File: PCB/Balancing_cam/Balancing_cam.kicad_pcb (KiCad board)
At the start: 4 copper layers, 50 x 50 mm, 123 parts, among them J1 JST_PH, J2 JST_PH, J3 USB_C_Receptacle_USB2.0_16P, J4 JST_XH, J5 Conn_01x04, J6 Conn_01x04, J7 Conn_01x04, J8 Conn_01x03, J9 Conn_01x04, Q1 BC817, SW1 SW_SPDT, SW2 EN, SW3 BOOT, U1 TMC2209-LA, U2 TMC2209-LA, U3 TPS62933, U4 TPS62933, U5 USBLC6-2P6, U6 LSM6DS3, U7 ESP32-S3-MINI-1

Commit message: Done, and completed bom
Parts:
- added TP1: TestPoint, TestPoint:TestPoint_Pad_D1.5mm, B.Cu at (141.1, 137.2)
- added TP10: TestPoint, TestPoint:TestPoint_Pad_D1.5mm, B.Cu at (139.4, 120.2)
- added TP11: TestPoint, TestPoint:TestPoint_Pad_D1.5mm, B.Cu at (136.2, 117.8)
- added TP12: TestPoint, TestPoint:TestPoint_Pad_D1.5mm, B.Cu at (109.8, 131.5)
- added TP13: TestPoint, TestPoint:TestPoint_Pad_D1.5mm, B.Cu at (109.0, 135.1)
- added TP14: TestPoint, TestPoint:TestPoint_Pad_D1.5mm, B.Cu at (126.2, 116.2)
- added TP15: TestPoint, TestPoint:TestPoint_Pad_D1.5mm, B.Cu at (107.8, 137.3)
- added TP16: TestPoint, TestPoint:TestPoint_Pad_D1.5mm, B.Cu at (130.3, 116.0)
- added TP17: TestPoint, TestPoint:TestPoint_Pad_D1.5mm, B.Cu at (128.4, 114.3)
- added TP18: TestPoint, TestPoint:TestPoint_Pad_D1.5mm, B.Cu at (115.0, 123.2)
- added TP19: TestPoint, TestPoint:TestPoint_Pad_D1.5mm, B.Cu at (115.0, 125.5)
- added TP2: TestPoint, TestPoint:TestPoint_Pad_D1.5mm, B.Cu at (141.1, 131.3)
- added TP21: TestPoint, TestPoint:TestPoint_Pad_D1.5mm, B.Cu at (114.3, 134.8)
- added TP22: TestPoint, TestPoint:TestPoint_Pad_D1.5mm, B.Cu at (121.6, 114.3)
- added TP23: TestPoint, TestPoint:TestPoint_Pad_D1.5mm, B.Cu at (123.8, 115.7)
- added TP3: TestPoint, TestPoint:TestPoint_Pad_D1.5mm, B.Cu at (120.0, 123.5)
- added TP4: TestPoint, TestPoint:TestPoint_Pad_D1.5mm, B.Cu at (132.5, 114.6)
- added TP5: TestPoint, TestPoint:TestPoint_Pad_D1.5mm, B.Cu at (146.8, 112.4)
- added TP6: TestPoint, TestPoint:TestPoint_Pad_D1.5mm, B.Cu at (132.5, 109.6)
- added TP7: TestPoint, TestPoint:TestPoint_Pad_D1.5mm, B.Cu at (132.5, 112.1)
- added TP8: TestPoint, TestPoint:TestPoint_Pad_D1.5mm, B.Cu at (108.7, 120.3)
- added TP9: TestPoint, TestPoint:TestPoint_Pad_D1.5mm, B.Cu at (108.7, 117.8)
- J1, J2: footprint Connector_JST:JST_PH_S2B-PH-SM4-TB_1x02-1MP_P2.00mm_Horizontal -> footprints:JST_PH_S2B-PH-SM4-TB_1x02-1MP_P2.00mm_Horizontal
- SW2: value EN -> B3U-1000P
- SW3: value BOOT -> B3U-1000P
- renumbered C45 to C29, C46 to C30, C29 to C31, C30 to C32, C31 to C33, C32 to C34, C33 to C35, C34 to C36, C35 to C37, C36 to C38, C37 to C39, C38 to C40, C39 to C41, C40 to C42, C41 to C43, C42 to C44, C43 to C45, C44 to C46, L9 to L10, L10 to L11, L11 to L12, L12 to L13, L13 to L14, L14 to L4, L4 to L5, L5 to L6, L6 to L7, L7 to L8, L8 to L9, R25 to R12, R12 to R13, R13 to R14, R14 to R15, R15 to R16, R16 to R17, R17 to R18, R18 to R19, R19 to R20, R20 to R21, R21 to R22, R22 to R23, R23 to R24, R24 to R25
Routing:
- net /Breakout/CTRL.TX: track 16.2 -> 20.1 mm, vias 0 -> 1
- net /Breakout/CTRL.RX: track 12.0 -> 15.9 mm, vias 0 -> 1
- net /Breakout/VTX.RX: track 16.8 -> 20.5 mm, vias 2 -> 3
- net /IMU/SCL: track 16.7 -> 19.7 mm, vias 0 -> 1
- net /IMU/INT1: track 10.6 -> 13.6 mm, vias 0 -> 1
- net Net-(Q1-C): track 2.98 -> 5.39 mm, vias 0 -> 1
- net /Breakout/VTX.TX: track 18.6 -> 20.9 mm, vias 2 -> 3
- net Net-(U6-CS): track 1.95 -> 4.05 mm, vias 0 -> 1
- net /IMU/SDA: track 15.9 -> 18.0 mm, vias 0 -> 1
- net /Microcontroller/MOT_1.UART: track 34.1 -> 36.2 mm
- net +5V: track 98.3 -> 99.9 mm
- net /Microcontroller/MOT_2.~{EN}: track 29.5 -> 30.9 mm
- net /Microcontroller/MOT_1.STEP: track 37.5 -> 38.9 mm
- net /Microcontroller/MOT_1.DIR: track 37.3 -> 38.7 mm
- net /Microcontroller/MOT_1.DIAG: track 34.7 -> 36.1 mm
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
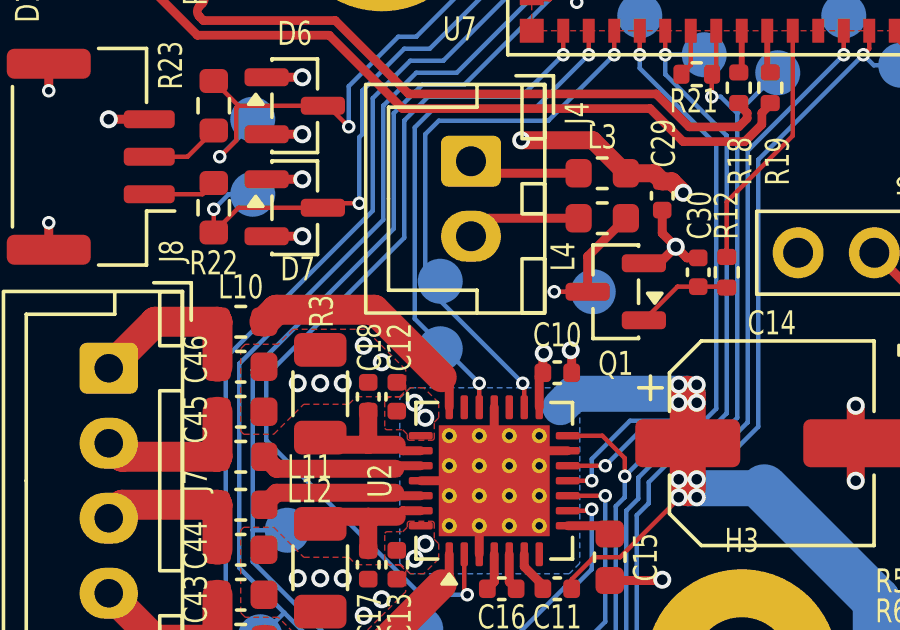
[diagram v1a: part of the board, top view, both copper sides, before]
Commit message: Fixed DRC errors
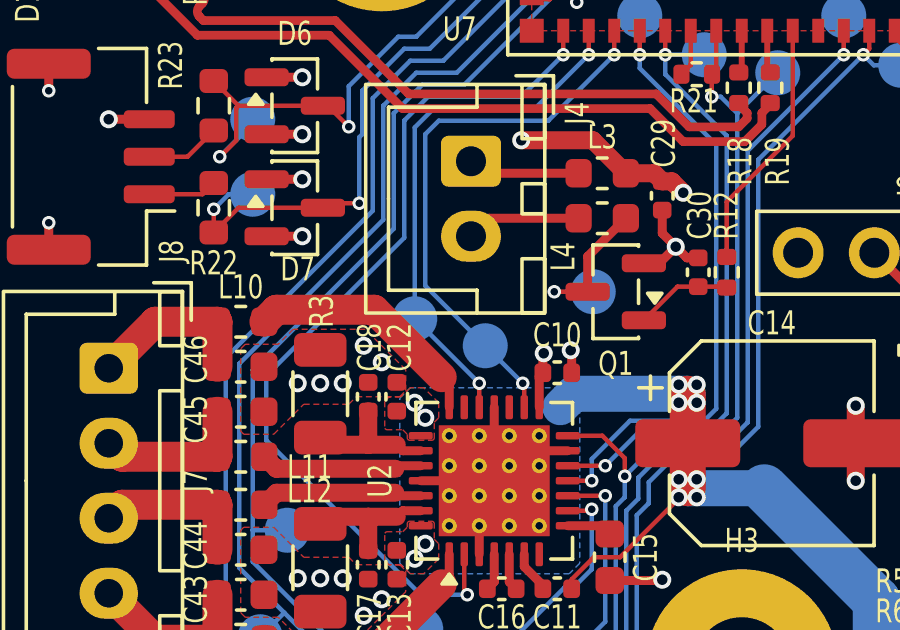
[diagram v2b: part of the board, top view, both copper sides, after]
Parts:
- moved TP18 2.62 mm to (116.5, 125.3)
- moved TP19 1.31 mm to (114.1, 124.5)
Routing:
- net Vdrive: vias 23 -> 24
- net /Microcontroller/MOT_2.DIR: vias 3 -> 2
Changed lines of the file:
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@@
 	(footprint "TestPoint:TestPoint_Pad_D1.5mm"
 		(layer "B.Cu")
-		(at 114.95 125.45 180)
+		(at 114.1 124.45 180)
 		(descr "SMD pad as test Point, diameter 1.5mm")
 		(tags "test point SMD pad")
@@
 	(footprint "TestPoint:TestPoint_Pad_D1.5mm"
 		(layer "B.Cu")
-		(at 114.95 123.2 180)
+		(at 116.45 125.35 180)
 		(descr "SMD pad as test Point, diameter 1.5mm")
 		(tags "test point SMD pad")
@@
 	)
 	(via
-		(at 114.1 127.25)
-		(size 0.6)
-		(drill 0.35)
-		(layers "F.Cu" "B.Cu")
-		(net "/Microcontroller/MOT_2.DIR")
-	)
-	(via
 		(at 116.25 126.6)
 		(size 0.45)
@@
 		(size 0.6)
 		(drill 0.35)
+		(layers "F.Cu" "B.Cu")
+		(net "Vdrive")
+	)
+	(via
+		(at 114.1 127.25)
+		(size 0.6)
+		(drill 0.35)

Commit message: Fixed Bom and added more GND fill
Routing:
- added copper zone on B.Cu, net GND
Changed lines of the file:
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@@
 		(layer "F.Cu")
 		(hatch edge 0.5)
-		(priority 14)
+		(priority 24)
 		(connect_pads yes
 			(clearance 0.2)
@@
 		(layer "F.Cu")
 		(hatch edge 0.5)
+		(priority 1)
 		(connect_pads yes
 			(clearance 0.2)
@@
 		(layer "F.Cu")
 		(hatch edge 0.5)
-		(priority 3)
+		(priority 9)
 		(connect_pads yes
 			(clearance 0.2)
@@
 		(layer "F.Cu")
 		(hatch edge 0.5)
+		(priority 2)
 		(connect_pads yes
 			(clearance 0.2)
@@
 		(layer "F.Cu")
 		(hatch edge 0.5)
-		(priority 11)
+		(priority 21)
 		(connect_pads yes
 			(clearance 0.2)
@@
 		(layer "F.Cu")
 		(hatch edge 0.5)
-		(priority 2)
+		(priority 7)
 		(connect_pads yes
 			(clearance 0.2)
@@
 		(layer "F.Cu")
 		(hatch edge 0.5)
-		(priority 10)
+		(priority 20)
 		(connect_pads yes
 			(clearance 0.2)
@@
 		(layer "F.Cu")
 		(hatch edge 0.5)
-		(priority 6)
+		(priority 13)
 		(connect_pads yes
 			(clearance 0.2)
@@
 		(layer "F.Cu")
 		(hatch edge 0.5)
-		(priority 9)
+		(priority 19)
 		(connect_pads yes
 			(clearance 0.2)
@@
 		(layer "F.Cu")
 		(hatch edge 0.5)
-		(priority 8)
+		(priority 15)
 		(connect_pads yes
 			(clearance 0.2)
@@
 		(layer "F.Cu")
 		(hatch edge 0.5)
-		(priority 13)
+		(priority 23)
 		(connect_pads yes
 			(clearance 0.2)
@@
 		(layer "F.Cu")
 		(hatch edge 0.5)
+		(priority 3)
 		(connect_pads yes
 			(clearance 0.2)
@@
 		(layer "F.Cu")
 		(hatch edge 0.5)
-		(priority 8)
+		(priority 16)
 		(connect_pads yes
 			(clearance 0.2)
@@
 		(layer "F.Cu")
 		(hatch edge 0.5)
-		(priority 4)
+		(priority 11)
 		(connect_pads yes
 			(clearance 0.2)
@@
 		(layer "F.Cu")
 		(hatch edge 0.5)
-		(priority 2)
+		(priority 8)
 		(connect_pads yes
 			(clearance 0.2)
@@
 		(layer "F.Cu")
 		(hatch edge 0.5)
-		(priority 8)
+		(priority 17)
 		(connect_pads yes
 			(clearance 0.2)
@@
 		(layer "F.Cu")
 		(hatch edge 0.5)
-		(priority 12)
+		(priority 22)
 		(connect_pads yes
 			(clearance 0.2)
@@
 		(layer "F.Cu")
 		(hatch edge 0.5)
-		(priority 8)
+		(priority 18)
 		(connect_pads yes
 			(clearance 0.2)
@@
 		(layer "F.Cu")
 		(hatch edge 0.5)
+		(priority 4)
 		(connect_pads yes
 			(clearance 0.2)
@@
 		(layer "F.Cu")
 		(hatch edge 0.5)
-		(priority 3)
+		(priority 10)
 		(connect_pads yes
 			(clearance 0.2)
@@
 	)
 	(zone
+		(net "GND")
+		(layers "F.Cu" "B.Cu")
+		(hatch edge 0.5)
+		(connect_pads
+			(clearance 0.2)
+		)
+		(min_thickness 0.2)
+		(fill yes
+			(thermal_gap 0.2)
+			(thermal_bridge_width 0.5)
+			(island_removal_mode 0)
+		)
+		(polygon
+			(pts
+				(xy 100.1 100.1) (xy 149.9 100.1) (xy 149.9 149.9) (xy 100.1 149.9)
+			)
+		)
+	)
+	(zone
 		(net "Vdrive")
 		(layer "B.Cu")
 		(hatch edge 0.5)
-		(priority 1)
+		(priority 5)
 		(connect_pads yes
 			(clearance 0.2)
@@
 		(layer "B.Cu")
 		(hatch edge 0.5)
-		(priority 1)
+		(priority 6)
 		(connect_pads yes
 			(clearance 0.2)
@@
 		(layer "In1.Cu")
 		(hatch edge 0.5)
-		(priority 5)
+		(priority 12)
 		(connect_pads
 			(clearance 0.2)
@@
 		(layer "In2.Cu")
 		(hatch edge 0.5)
-		(priority 7)
+		(priority 14)
 		(connect_pads
 			(clearance 0.2)

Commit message: Fixed small errors and routing issues
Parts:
- moved TP16 1.77 mm to (129.1, 117.2)
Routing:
- net +5V: track 99.9 -> 132.1 mm, vias 13 -> 12
- net /Microcontroller/IO21: track 8.45 -> 10.5 mm, vias 0 -> 2
- net GND: track 69.5 -> 67.8 mm
- net Vdrive: track 48.4 -> 50.0 mm
- net /Breakout/CTRL.RX: track 15.9 -> 14.6 mm

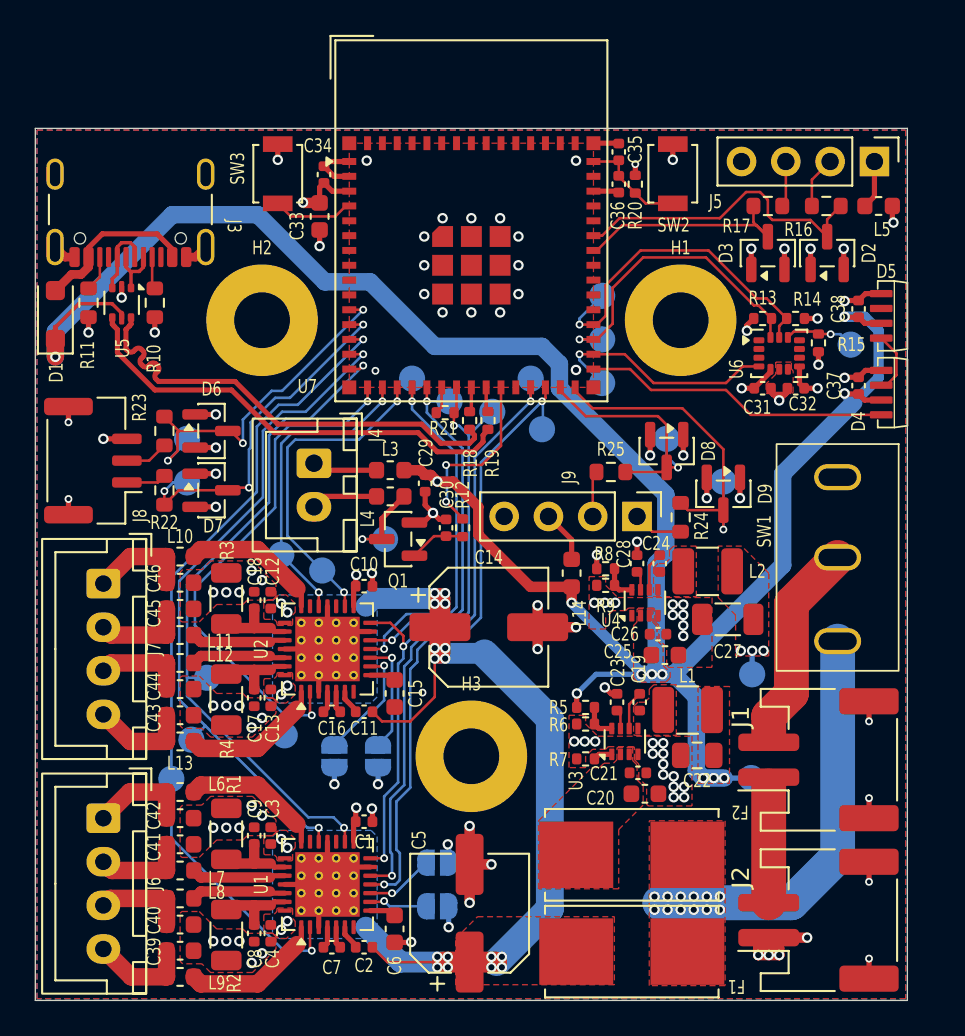
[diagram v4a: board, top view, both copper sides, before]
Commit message: Fixed traces on the pcb
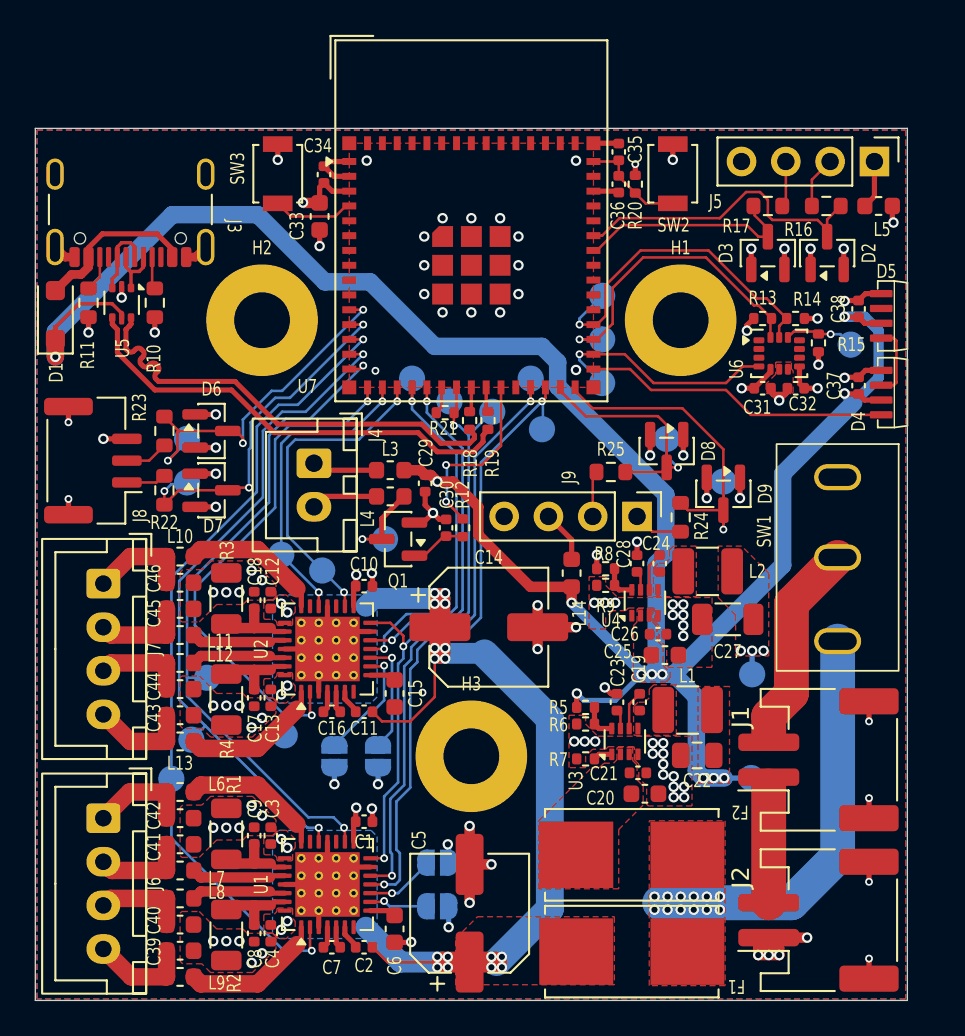
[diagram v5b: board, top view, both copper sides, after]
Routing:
- net Net-(D4-DOUT): track 3.60 -> 4.27 mm
